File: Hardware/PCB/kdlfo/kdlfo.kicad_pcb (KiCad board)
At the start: 2 copper layers, 93 x 61 mm, 55 parts, among them J1 Synth_power_2x5, J10 AudioJack2, J11 AudioJack2, J12 2 PIN MOLEX HEADER, J13 2 PIN MOLEX CONNECTOR, J2 2 PIN MOLEX HEADER, J3 2 PIN MOLEX HEADER, J4 AudioJack2, J5 2 PIN MOLEX HEADER, J6 2 PIN MOLEX CONNECTOR, J7 2 PIN MOLEX CONNECTOR, J8 2 PIN MOLEX CONNECTOR, J9 3 POSITION PIN HEADER, Q1 J201, Q2 J201, U1 TL074, U2 TL074

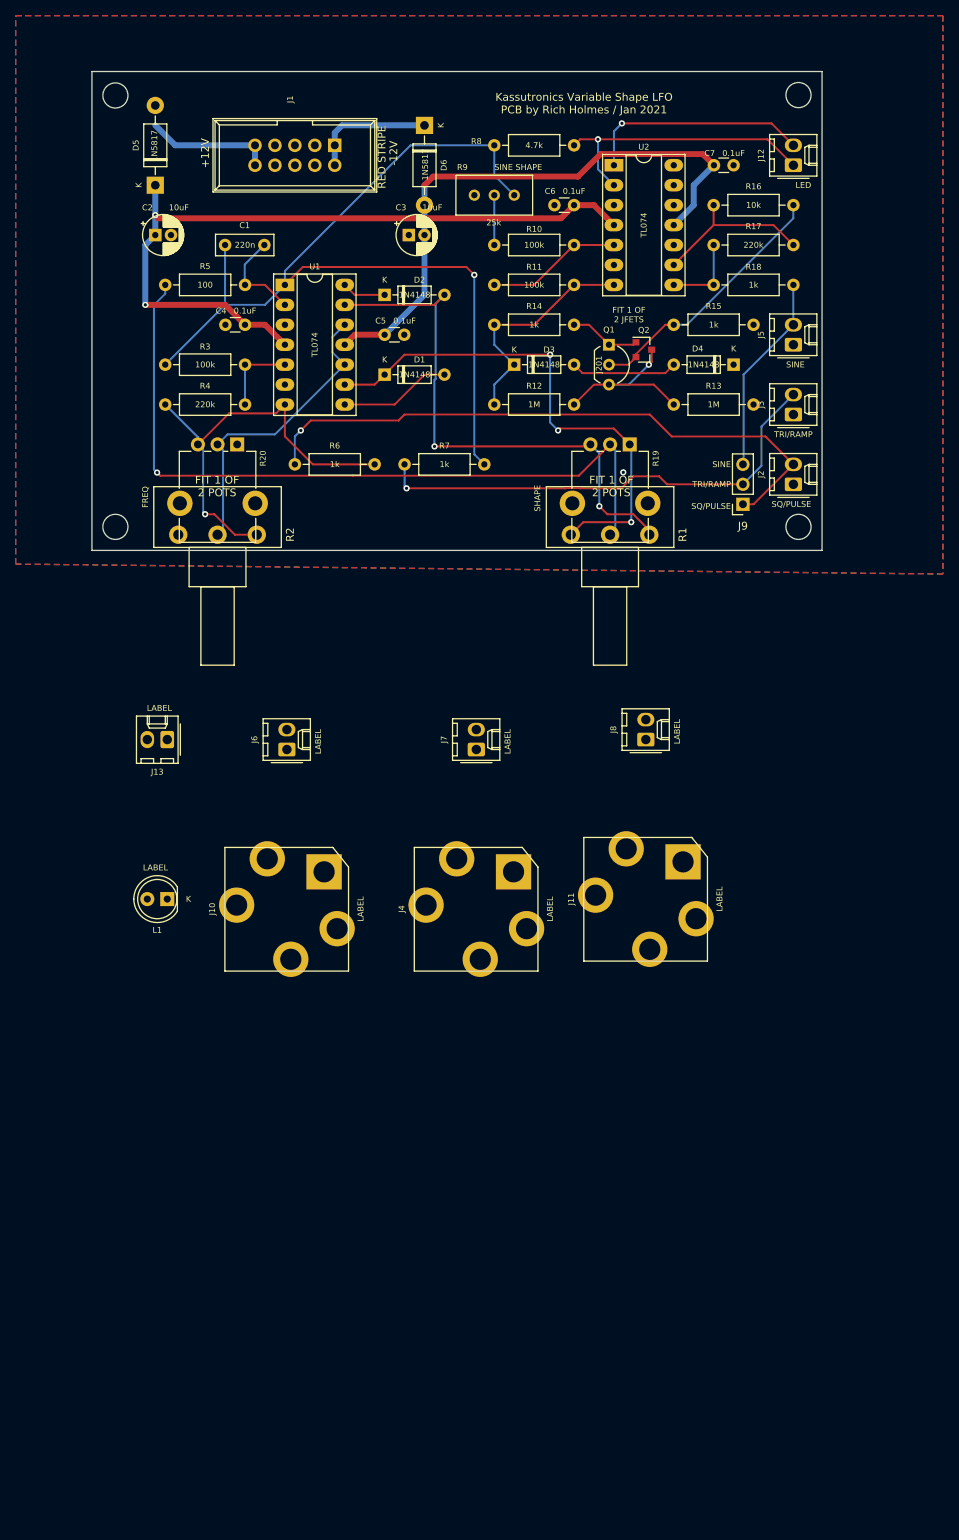
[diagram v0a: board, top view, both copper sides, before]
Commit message: Better .gitignore; rm extraneous footprint library; misc revisions
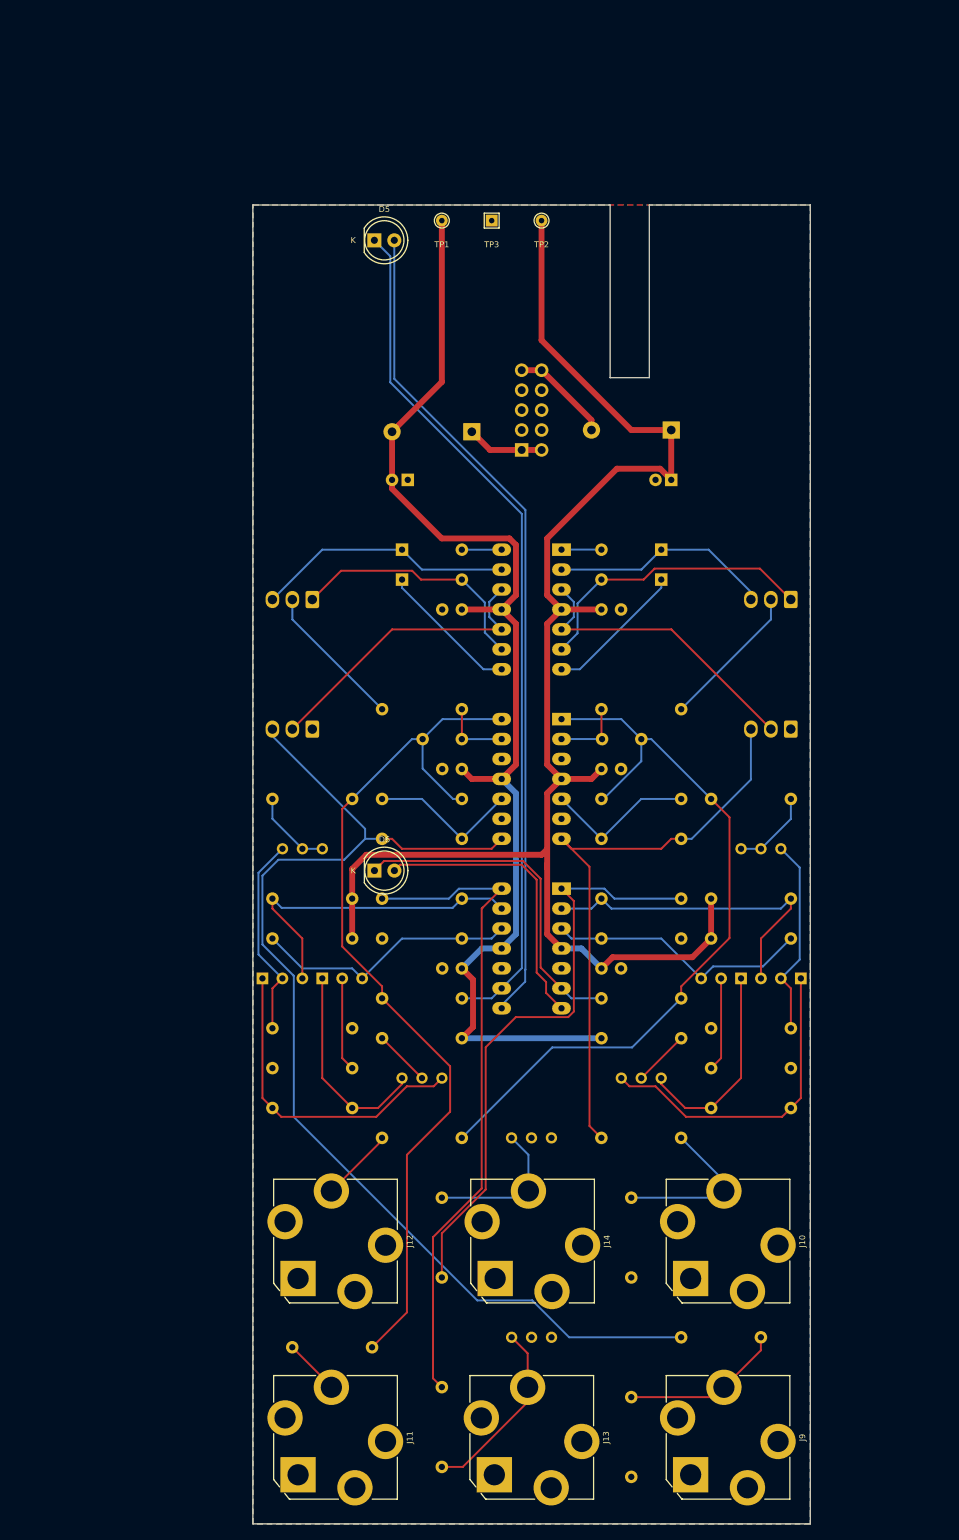
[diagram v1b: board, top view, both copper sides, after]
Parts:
- removed J2: 2 PIN MOLEX HEADER, ao_tht:Molex_KK-254_AE-6410-02A_1x02_P2.54mm_Vertical
- removed J4: AudioJack2, ao_tht:Jack_6.35mm_PJ_629HAN
- removed J6, J8: 2 PIN MOLEX CONNECTOR, ao_tht:Molex_KK-254_AE-6410-02A_1x02_P2.54mm_Vertical
- removed L1: LED_Dual_2pin, ao_tht:LED_D5.0mm
- removed REF** (x4): MountingHole_3.2mm_M3, ao_tht:MountingHole_3.2mm_M3
- added C10: 100nF, ao_tht:C_Disc_D3.0mm_W1.6mm_P2.50mm, B.Cu at (88.6, 130.2)
- added C8: 0.1uF, ao_tht:C_Disc_D3.0mm_W1.6mm_P2.50mm, B.Cu at (88.6, 84.5)
- added C9: 0.1uF, ao_tht:C_Disc_D3.0mm_W1.6mm_P2.50mm, B.Cu at (88.6, 104.8)
- added D7: 1N5817, ao_tht:D_DO-41_SOD81_P10.16mm_Horizontal, B.Cu at (117.8, 61.7)
- added D8: 1N5817, ao_tht:D_DO-41_SOD81_P10.16mm_Horizontal, B.Cu at (92.4, 61.9)
- added GRAF1: Holes, kdlfo:kdlfo_panel_holes, F.Cu at (100.0, 115.0)
- added J14: AudioJack2, ao_tht:Jack_6.35mm_PJ_629HAN, F.Cu at (100.1, 165.0)
- added J15: Synth_power_2x5, ao_tht:Power_Header, B.Cu at (98.7, 64.2)
- added Q3: 2N3904, ao_tht:TO-92_Inline_Wide, B.Cu at (134.3, 131.5)
- added Q4: 2N3904, ao_tht:TO-92_Inline_Wide, B.Cu at (126.7, 131.5)
- added R21: 47k, ao_tht:R_Axial_DIN0207_L6.3mm_D2.5mm_P10.16mm_Horizontal, B.Cu at (67.0, 108.7)
- added R22: 47k, ao_tht:R_Axial_DIN0207_L6.3mm_D2.5mm_P10.16mm_Horizontal, B.Cu at (133.0, 108.7)
- added R23: 20k, ao_tht:R_Axial_DIN0207_L6.3mm_D2.5mm_P10.16mm_Horizontal, B.Cu at (91.1, 126.4)
- added R24: 2k, ao_tht:R_Axial_DIN0207_L6.3mm_D2.5mm_P10.16mm_Horizontal, B.Cu at (88.6, 193.7)
- added R25: 20k, ao_tht:R_Axial_DIN0207_L6.3mm_D2.5mm_P10.16mm_Horizontal, B.Cu at (108.9, 126.4)
- added R26: 2k, ao_tht:R_Axial_DIN0207_L6.3mm_D2.5mm_P10.16mm_Horizontal, B.Cu at (88.6, 159.4)
- added R27: 2.2k, ao_tht:R_Axial_DIN0207_L6.3mm_D2.5mm_P10.16mm_Horizontal, B.Cu at (67.0, 137.9)
- added R28: 2.2k, ao_tht:R_Axial_DIN0207_L6.3mm_D2.5mm_P10.16mm_Horizontal, B.Cu at (77.2, 142.9)
- added R29: 2.2k, ao_tht:R_Axial_DIN0207_L6.3mm_D2.5mm_P10.16mm_Horizontal, B.Cu at (133.0, 137.9)
- added R30: 2.2k, ao_tht:R_Axial_DIN0207_L6.3mm_D2.5mm_P10.16mm_Horizontal, B.Cu at (122.9, 142.9)
- added R31: 390R, ao_tht:R_Axial_DIN0207_L6.3mm_D2.5mm_P10.16mm_Horizontal, B.Cu at (77.2, 148.0)
- added R32: 390R, ao_tht:R_Axial_DIN0207_L6.3mm_D2.5mm_P10.16mm_Horizontal, B.Cu at (122.9, 148.0)
- added R33: 18k, ao_tht:R_Axial_DIN0207_L6.3mm_D2.5mm_P10.16mm_Horizontal, B.Cu at (91.1, 139.1)
- added R34: 18k, ao_tht:R_Axial_DIN0207_L6.3mm_D2.5mm_P10.16mm_Horizontal, B.Cu at (108.9, 139.1)
- added RV10: B50k, ao_tht:Potentiometer_Bourns_3296W_Vertical_standard, B.Cu at (111.4, 144.2)
- added RV5: B50K, ao_tht:Potentiometer_Bourns_3296W_Vertical_standard, B.Cu at (73.3, 115.0)
- added RV6: B50K, ao_tht:Potentiometer_Bourns_3296W_Vertical_standard, B.Cu at (126.7, 115.0)
- added RV7: B5K, ao_tht:Potentiometer_Bourns_3296W_Vertical_standard, B.Cu at (97.5, 177.2)
- added RV8: B5K, ao_tht:Potentiometer_Bourns_3296W_Vertical_standard, B.Cu at (97.5, 151.8)
- added RV9: B50k, ao_tht:Potentiometer_Bourns_3296W_Vertical_standard, B.Cu at (88.6, 144.2)
- added TP1: -12V, ao_tht:TestPoint_THTPad_D1.5mm_Drill0.7mm, F.Cu at (88.6, 35.0)
- added TP2: +12V, ao_tht:TestPoint_THTPad_D1.5mm_Drill0.7mm, F.Cu at (101.3, 35.0)
- added TP3: GND, ao_tht:TestPoint_THTPad_1.5x1.5mm_Drill0.7mm, F.Cu at (94.9, 35.0)
- added U3: TL074, ao_tht:DIP-14_W7.62mm_Socket_LongPads, B.Cu at (103.8, 120.1)
- C1, C3, C4, C5, D1, D2, D3, D4, R16, R4, U1, U2: moved to B.Cu
- C2: value 10uF -> 220n; footprint ao_tht:CP_Radial_D5.0mm_P2.00mm -> ao_tht:C_Rect_L7.2mm_W2.5mm_P5.00mm_FKS2_FKP2_MKS2_MKP2; moved to B.Cu
- C6: value 0.1uF -> 100nF; moved to B.Cu
- C7: value 0.1uF -> 10uF; footprint ao_tht:C_Disc_D3.0mm_W1.6mm_P2.50mm -> ao_tht:CP_Radial_D5.0mm_P2.00mm; moved to B.Cu
- D5, D6: value 1N5817 -> LED_Dual_2pin; footprint ao_tht:D_DO-41_SOD81_P10.16mm_Horizontal -> ao_tht:LED_D5.0mm
- J1: value Synth_power_2x5 -> 3_pin_Molex_header; footprint ao_tht:Power_Header -> ao_tht:Molex_KK-254_AE-6410-03A_1x03_P2.54mm_Vertical; moved to B.Cu
- J12: value 2 PIN MOLEX HEADER -> AudioJack2; footprint ao_tht:Molex_KK-254_AE-6410-02A_1x02_P2.54mm_Vertical -> ao_tht:Jack_6.35mm_PJ_629HAN
- J13: value 2 PIN MOLEX CONNECTOR -> AudioJack2; footprint ao_tht:Molex_KK-254_AE-6410-02A_1x02_P2.54mm_Vertical -> ao_tht:Jack_6.35mm_PJ_629HAN
- J3, J5: value 2 PIN MOLEX HEADER -> 3_pin_Molex_header; footprint ao_tht:Molex_KK-254_AE-6410-02A_1x02_P2.54mm_Vertical -> ao_tht:Molex_KK-254_AE-6410-03A_1x03_P2.54mm_Vertical; moved to B.Cu
- J7: value 2 PIN MOLEX CONNECTOR -> 3_pin_Molex_header; footprint ao_tht:Molex_KK-254_AE-6410-02A_1x02_P2.54mm_Vertical -> ao_tht:Molex_KK-254_AE-6410-03A_1x03_P2.54mm_Vertical; moved to B.Cu
- J9: value 3 POSITION PIN HEADER -> AudioJack2; footprint Connector_PinSocket_2.54mm:PinSocket_1x03_P2.54mm_Vertical -> ao_tht:Jack_6.35mm_PJ_629HAN
- Q1: value J201 -> 2N3904; moved to B.Cu
- Q2: value J201 -> 2N3904; footprint Package_TO_SOT_SMD:SOT-23 -> ao_tht:TO-92_Inline_Wide; moved to B.Cu
- R1: value B100k -> 100; footprint Potentiometer_THT:Potentiometer_Piher_T-16H_Single_Horizontal -> ao_tht:R_Axial_DIN0207_L6.3mm_D2.5mm_P10.16mm_Horizontal; moved to B.Cu
- R10: value 100k -> 2.2k; moved to B.Cu
- R11: value 100k -> 1k; moved to B.Cu
- R12: value 1M -> 1k; moved to B.Cu
- R13: value 1M -> 4.7k; moved to B.Cu
- R14: value 1k -> 4.7k; moved to B.Cu
- R15, R18: value 1k -> 10k; moved to B.Cu
- R17: value 220k -> 20k; moved to B.Cu
- R19: value B100k -> 10k; footprint ao_tht:Potentiometer_Alpha_RD901F-40-00D_Single_Vertical_CircularHoles -> ao_tht:R_Axial_DIN0207_L6.3mm_D2.5mm_P10.16mm_Horizontal; moved to B.Cu
- R2: value A100k -> 100; footprint Potentiometer_THT:Potentiometer_Piher_T-16H_Single_Horizontal -> ao_tht:R_Axial_DIN0207_L6.3mm_D2.5mm_P10.16mm_Horizontal; moved to B.Cu
- R20: value B100k -> 20k; footprint ao_tht:Potentiometer_Alpha_RD901F-40-00D_Single_Vertical_CircularHoles -> ao_tht:R_Axial_DIN0207_L6.3mm_D2.5mm_P10.16mm_Horizontal; moved to B.Cu
- R3: value 100k -> 220k; moved to B.Cu
- R5: value 100 -> 2.7k; moved to B.Cu
- R6: value 1k -> 2.7k; moved to B.Cu
- R7: value 1k -> 100k; moved to B.Cu
- R8: value 4.7k -> 2.2k; moved to B.Cu
- R9: value 25k -> 100k; footprint ao_tht:Potentiometer_Bourns_3296W_Vertical -> ao_tht:R_Axial_DIN0207_L6.3mm_D2.5mm_P10.16mm_Horizontal; moved to B.Cu
- moved R8 159.6 mm to (112.7, 184.8), turned to -90 degrees
- moved R5 154.0 mm to (129.2, 177.2), turned to 180 degrees
- moved J12 149.0 mm to (75.0, 165.0), turned to -90 degrees
- moved R11 140.0 mm to (69.5, 178.5), turned to 0 degrees
- moved R10 121.6 mm to (112.7, 159.4), turned to -90 degrees
- moved J9 118.9 mm to (125.0, 190.0), turned to -90 degrees
- moved R16 104.1 mm to (77.2, 126.4), turned to 180 degrees
- moved J13 100.3 mm to (100.0, 190.0), turned to -90 degrees
- moved R6 98.9 mm to (119.0, 151.8), turned to 180 degrees
- moved C6 97.3 mm to (108.9, 130.2), turned to 0 degrees
- moved D6 95.1 mm to (80.0, 117.8), turned to 0 degrees
- moved R12 94.5 mm to (81.0, 151.8)
- moved R17 93.4 mm to (81.0, 121.4)
- moved Q1 92.0 mm to (65.7, 131.5), turned to 0 degrees
- moved Q2 89.9 mm to (73.3, 131.5)
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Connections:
- C2 pad 1: +12V -> Net-(C2-Pad1)
- C2 pad 2: GND -> Net-(C2-Pad2)
- C3 pad 1: GND -> +12V
- C3 pad 2: -12V -> GND
- C5 pad 1: GND -> +12V
- C5 pad 2: -12V -> GND
- D1 pad 1: Net-(D1-Pad1) -> SHPOTCW
- D2 pad 1: Net-(D2-Pad1) -> SHPOTCW_A
- D3 pad 2: Net-(D3-Pad2) -> SHPOTCCW
- D4 pad 1: GND -> Net-(D4-Pad1)
- D4 pad 2: Net-(D3-Pad2) -> SHPOTCCW_A
- D5 pad 1: +12V -> Net-(D5-Pad1)
- D5 pad 2: /+12_IN -> Net-(D5-Pad2)
- D6 pad 1: /-12_IN -> Net-(D6-Pad1)
- D6 pad 2: -12V -> Net-(D6-Pad2)
- J1 pad 1: /-12_IN -> SHPOTCCW
- J1 pad 2: /-12_IN -> SHPOTW
- J1 pad 3: GND -> SHPOTCW
- J10 pad S: GND1 -> GND
- J10 pad T: /TRIRAMP_P -> /SQPULSE_A
- J11 pad S: GND1 -> GND
- J11 pad T: /SINE_P -> /TRIRAMP
- J3 pad 1: GND -> SHPOTCCW_A
- J3 pad 2: /TRIRAMP -> SHPOTW_A
- J5 pad 2: /SINE -> FRPOTW
- J7 pad 1: /SQPULSE_P -> GND
- J7 pad 2: GND1 -> FRPOTW_A
- Q2 pad 1: Net-(Q1-Pad1) -> Net-(Q2-Pad1)
- Q2 pad 2: Net-(Q1-Pad2) -> Net-(Q2-Pad2)
- Q2 pad 3: Net-(Q1-Pad3) -> Net-(Q2-Pad3)
- R1 pad 1: Net-(D1-Pad1) -> SHPOTW
- R1 pad 2: Net-(R1-Pad2) -> Net-(C1-Pad2)
- R10 pad 1: Net-(R10-Pad1) -> /SQPULSE_A
- R10 pad 2: Net-(R10-Pad2) -> GND
- R11 pad 1: Net-(D3-Pad1) -> /TRIRAMP
- R11 pad 2: Net-(R10-Pad1) -> Net-(C1-Pad1)
- R12 pad 1: Net-(D3-Pad1) -> /TRIRAMP_A
- R12 pad 2: Net-(Q1-Pad3) -> Net-(C2-Pad1)
- R13 pad 1: Net-(Q1-Pad3) -> Net-(D5-Pad1)
- R13 pad 2: GND -> Net-(C1-Pad1)
- R14 pad 1: Net-(D3-Pad1) -> Net-(D6-Pad1)
- R14 pad 2: Net-(Q1-Pad1) -> Net-(C2-Pad1)
- R15 pad 1: Net-(Q1-Pad2) -> +12V
- R15 pad 2: GND -> Net-(Q1-Pad3)
- R16 pad 1: Net-(R16-Pad1) -> +12V
- R16 pad 2: Net-(Q1-Pad2) -> Net-(Q2-Pad3)
- R17 pad 2: Net-(R16-Pad1) -> Net-(Q1-Pad3)
- R18 pad 1: /SINE -> +12V
- R18 pad 2: Net-(R17-Pad1) -> Net-(Q3-Pad3)
- R19 pad 1: Net-(D1-Pad1) -> +12V
- R19 pad 2: Net-(R1-Pad2) -> Net-(Q4-Pad3)
- R2 pad 1: GND -> SHPOTW_A
- R2 pad 2: Net-(R2-Pad2) -> Net-(C2-Pad2)
- R20 pad 1: GND -> Net-(R20-Pad1)
- R20 pad 2: Net-(R2-Pad2) -> Net-(Q3-Pad3)
- R3 pad 1: Net-(R3-Pad1) -> FRPOTCW
- R3 pad 2: Net-(C1-Pad1) -> Net-(R3-Pad2)
- R4 pad 1: Net-(R2-Pad3) -> FRPOTCW_A
- R4 pad 2: Net-(R3-Pad1) -> Net-(R4-Pad2)
- R5 pad 1: Net-(R1-Pad2) -> /SQPULSE
- R5 pad 2: Net-(C1-Pad2) -> FRPOTCW
- R6 pad 1: /SQPULSE -> /SQPULSE_A
- R6 pad 2: Net-(R2-Pad3) -> FRPOTCW_A
- R7 pad 1: /TRIRAMP -> Net-(R3-Pad2)
- R8 pad 1: /LED -> /SQPULSE
- R8 pad 2: Net-(C1-Pad1) -> GND
- R9 pad 1: Net-(C1-Pad1) -> Net-(R4-Pad2)
- R9 pad 2: Net-(R10-Pad2) -> Net-(C2-Pad1)
- U1 pad 1: Net-(C1-Pad1) -> Net-(D2-Pad2)
- U1 pad 10: Net-(R2-Pad2) -> FRPOTW
- U1 pad 12: Net-(R2-Pad2) -> FRPOTW
- U1 pad 13: Net-(D2-Pad2) -> SHPOTCW
- U1 pad 14: Net-(D2-Pad1) -> Net-(D1-Pad2)
- U1 pad 2: Net-(C1-Pad2) -> SHPOTCW_A
- U1 pad 3: GND -> FRPOTW_A
- U1 pad 5: Net-(R3-Pad1) -> FRPOTW_A
- U1 pad 6: GND -> SHPOTCCW_A
- U1 pad 7: Net-(R2-Pad3) -> Net-(D4-Pad1)
- U1 pad 8: Net-(D1-Pad2) -> Net-(D3-Pad1)
- U1 pad 9: Net-(D1-Pad1) -> SHPOTCCW
- U2 pad 1: Net-(J12-Pad2) -> Net-(C2-Pad1)
- U2 pad 10: GND -> Net-(R3-Pad2)
- U2 pad 12: (no net) -> GND
- U2 pad 13: (no net) -> Net-(C1-Pad2)
- U2 pad 14: (no net) -> Net-(C1-Pad1)
- U2 pad 2: /LED -> Net-(C2-Pad2)
- U2 pad 5: Net-(R10-Pad1) -> Net-(R4-Pad2)
- U2 pad 7: Net-(D3-Pad1) -> FRPOTCW_A
- U2 pad 8: Net-(R17-Pad1) -> FRPOTCW
- U2 pad 9: Net-(R16-Pad1) -> GND
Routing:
- net FRPOTCW: track 0.00 -> 145.7 mm
- net Net-(D5-Pad1): track 0.00 -> 109.7 mm
- net Net-(D5-Pad2): track 0.00 -> 106.0 mm
- net Net-(C2-Pad1): track 0.00 -> 97.4 mm
- net Net-(R1-Pad2): track 96.2 -> 0.00 mm, vias 1 -> 0
- net +12V: track 96.0 -> 191.2 mm, vias 2 -> 0
- net -12V: track 75.6 -> 155.3 mm
- net Net-(R20-Pad1): track 0.00 -> 76.8 mm
- net FRPOTCW_A: track 0.00 -> 74.9 mm
- net Net-(R17-Pad1): track 10.2 -> 83.4 mm
- net Net-(D1-Pad1): track 66.8 -> 0.00 mm, vias 3 -> 0
- net Net-(D2-Pad2): track 69.6 -> 5.09 mm, vias 2 -> 0
- net /SQPULSE: track 79.4 -> 20.6 mm, vias 1 -> 0
- net /TRIRAMP: track 61.3 -> 7.16 mm, vias 1 -> 0
- net Net-(R2-Pad3): track 53.9 -> 0.00 mm, vias 1 -> 0
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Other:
- board size 93 x 61 mm -> 71 x 168 mm
- board text removed: "FIT 1 OF 2 JFETS"
- board text removed: "FIT 1 OF 2 POTS"
- board text removed: "Kassutronics Variable Shape LFO PCB by Rich Holmes / Jan 2021"
- board text removed: "SINE"
- board text removed: "SQ/PULSE"
- board text removed: "TRI/RAMP"

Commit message: Reorg schematic, redo layout
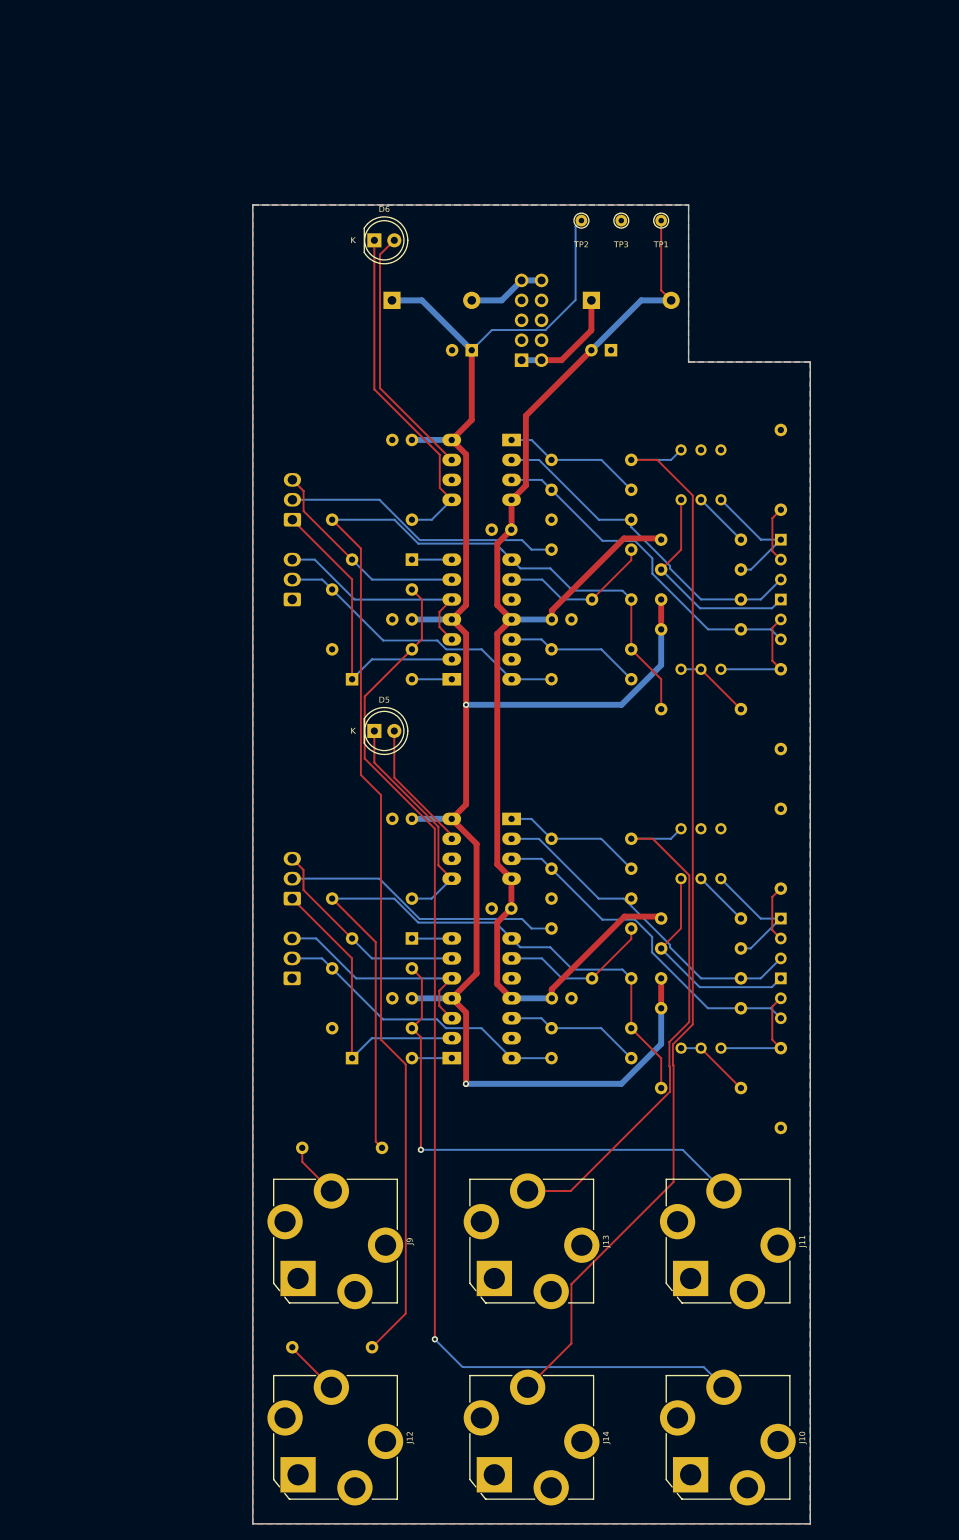
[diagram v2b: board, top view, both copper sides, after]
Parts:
- removed J5: 3_pin_Molex_header, ao_tht:Molex_KK-254_AE-6410-03A_1x03_P2.54mm_Vertical
- added C11: 0.1uF, ao_tht:C_Disc_D3.0mm_W1.6mm_P2.50mm, B.Cu at (84.8, 134.1)
- added C12: 0.1uF, ao_tht:C_Disc_D3.0mm_W1.6mm_P2.50mm, B.Cu at (105.1, 134.1)
- added J2: 3_pin_Molex_header, ao_tht:Molex_KK-254_AE-6410-03A_1x03_P2.54mm_Vertical, B.Cu at (69.5, 131.5)
- added U4: TL072, ao_tht:DIP-8_W7.62mm_Socket_LongPads, B.Cu at (97.5, 111.2)
- C1, C2: footprint ao_tht:C_Rect_L7.2mm_W2.5mm_P5.00mm_FKS2_FKP2_MKS2_MKP2 -> ao_tht:C_Rect_L7.2mm_W7.2mm_P5.00mm_FKS2_FKP2_MKS2_MKP2
- C10, C6: value 100nF -> 0.1uF
- C3, C7: footprint ao_tht:CP_Radial_D5.0mm_P2.00mm -> ao_tht:CP_Radial_D6.3mm_P2.50mm
- D1, D2, D3, D4: footprint ao_tht:D_DO-35_SOD27_P7.62mm_Horizontal -> Diode_THT:D_DO-35_SOD27_P7.62mm_Horizontal
- R1: value 100 -> 47k
- R11: value 1k -> 100k
- R13: value 4.7k -> 10k
- R15: value 10k -> 18k
- R16: value 10k -> 2.2k
- R17: value 20k -> 220k
- R21: value 47k -> 20k
- R23: value 20k -> 2.7k
- R24: value 2k -> 20k
- R28: value 2.2k -> 4.7k
- R3: value 220k -> 100
- R31: value 390R -> 1k
- R33: value 18k -> 2k
- R5: value 2.7k -> 2.2k
- R7: value 100k -> 10k
- R8: value 2.2k -> 390R
- RV7: value B5K -> B50k
- RV9: value B50k -> B5K
- TP3: footprint ao_tht:TestPoint_THTPad_1.5x1.5mm_Drill0.7mm -> ao_tht:TestPoint_THTPad_D1.5mm_Drill0.7mm
- U2: value TL074 -> TL072; footprint ao_tht:DIP-14_W7.62mm_Socket_LongPads -> ao_tht:DIP-8_W7.62mm_Socket_LongPads
- moved R26 97.0 mm to (112.7, 65.5), turned to 180 degrees
- moved RV8 90.3 mm to (119.0, 64.2)
- moved D6 80.3 mm to (80.0, 37.5)
- moved R24 79.9 mm to (112.7, 117.5), turned to 180 degrees
- moved R6 77.8 mm to (84.8, 82.0)
- moved R10 75.2 mm to (84.8, 89.6), turned to 180 degrees
- moved RV10 74.1 mm to (119.0, 70.5)
- moved R30 71.7 mm to (131.8, 71.8), turned to 90 degrees
- moved R32 68.7 mm to (126.7, 79.4), turned to 180 degrees
- moved R1 66.5 mm to (126.7, 145.5), turned to 180 degrees
- moved Q1 66.0 mm to (131.8, 131.5), turned to -90 degrees
- moved J7 65.6 mm to (69.5, 83.2), turned to 90 degrees
- moved R14 65.6 mm to (84.8, 73.1), turned to 180 degrees
- moved D1 65.1 mm to (77.1, 141.7)
- moved J3 64.3 mm to (69.5, 73.1), turned to 90 degrees
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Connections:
- net /SINE_A renamed /LFO A/SINE
- net /SINE_ROUND_A renamed /LFO A/SINE_ROUND
- net /SINE_SYM_A renamed /LFO A/SINE_SYM
- net /SQPULSE_A renamed /LFO A/SQPULSE
- net /TRIRAMP_A renamed /LFO A/TRIRAMP
- net SHPOTW_A renamed /LFO A/SHPOTW
- C6 pad 1: +12V -> GND
- C6 pad 2: GND -> -12V
- C9 pad 1: GND -> +12V
- C9 pad 2: -12V -> GND
- D1 pad 1: SHPOTCW -> /LFO B/SHPOTCW
- D2 pad 1: SHPOTCW_A -> /LFO A/SHPOTCW
- D3 pad 2: SHPOTCCW -> /LFO B/SHPOTCCW
- D4 pad 2: SHPOTCCW_A -> /LFO A/SHPOTCCW
- J1 pad 1: SHPOTCCW -> /LFO B/SHPOTCW
- J1 pad 2: SHPOTW -> /LFO B/SHPOTW
- J1 pad 3: SHPOTCW -> /LFO B/SHPOTCCW
- J11 pad T: /TRIRAMP -> /LFO B/SQPULSE
- J13 pad T: /SINE -> /LFO B/SINE
- J3 pad 1: SHPOTCCW_A -> /LFO A/SHPOTCW
- J3 pad 3: SHPOTCW_A -> /LFO A/SHPOTCCW
- J7 pad 2: FRPOTW_A -> /LFO A/FRPOTCW
- J7 pad 3: FRPOTCW_A -> /LFO A/FRPOTW
- J9 pad T: /SQPULSE -> /LFO B/TRIRAMP
- R1 pad 1: SHPOTW -> /LFO B/SINE_ROUND
- R1 pad 2: Net-(C1-Pad2) -> Net-(C1-Pad1)
- R11 pad 1: /TRIRAMP -> Net-(R11-Pad1)
- R13 pad 1: Net-(D5-Pad1) -> +12V
- R13 pad 2: Net-(C1-Pad1) -> Net-(Q2-Pad3)
- R15 pad 1: +12V -> -12V
- R15 pad 2: Net-(Q1-Pad3) -> /LFO B/SINE_SYM
- R16 pad 1: +12V -> Net-(Q2-Pad2)
- R16 pad 2: Net-(Q2-Pad3) -> GND
- R17 pad 1: Net-(R17-Pad1) -> /LFO B/FRPOTCW
- R17 pad 2: Net-(Q1-Pad3) -> Net-(R11-Pad1)
- R21 pad 1: /SINE_ROUND -> Net-(Q2-Pad3)
- R21 pad 2: Net-(C1-Pad1) -> GND
- R23 pad 1: Net-(Q2-Pad3) -> /LFO B/SQPULSE
- R23 pad 2: GND -> /LFO B/FRPOTCW
- R24 pad 1: /SINE -> Net-(R24-Pad1)
- R24 pad 2: Net-(R17-Pad1) -> Net-(Q1-Pad3)
- R27 pad 1: Net-(Q1-Pad2) -> /LFO B/SQPULSE
- R28 pad 1: Net-(Q2-Pad2) -> Net-(D5-Pad1)
- R28 pad 2: GND -> Net-(C1-Pad1)
- R3 pad 1: FRPOTCW -> /LFO B/SHPOTW
- R3 pad 2: Net-(R3-Pad2) -> Net-(C1-Pad2)
- R31 pad 1: Net-(Q2-Pad1) -> /LFO B/TRIRAMP
- R31 pad 2: Net-(Q1-Pad1) -> Net-(C1-Pad1)
- R33 pad 1: -12V -> /LFO B/SINE
- R33 pad 2: /SINE_SYM -> Net-(R24-Pad1)
- R4 pad 1: FRPOTCW_A -> /LFO A/FRPOTCW
- R5 pad 1: /SQPULSE -> Net-(Q1-Pad2)
- R5 pad 2: FRPOTCW -> GND
- R6 pad 2: FRPOTCW_A -> /LFO A/FRPOTCW
- R7 pad 1: Net-(R3-Pad2) -> +12V
- R7 pad 2: Net-(C1-Pad1) -> Net-(Q1-Pad3)
- R8 pad 1: /SQPULSE -> Net-(Q2-Pad1)
- R8 pad 2: GND -> Net-(Q1-Pad1)
- RV5 pad 1: /SINE_ROUND -> /LFO B/SINE_ROUND
- RV5 pad 2: /SINE_ROUND -> /LFO B/SINE_ROUND
- RV7 pad 1: /SINE -> Net-(Q1-Pad1)
- RV7 pad 2: GND -> /LFO B/SINE_SYM
- RV7 pad 3: GND -> Net-(Q2-Pad1)
- RV9 pad 1: Net-(Q1-Pad1) -> /LFO B/SINE
- RV9 pad 2: /SINE_SYM -> GND
- RV9 pad 3: Net-(Q2-Pad1) -> GND
- U1 pad 10: FRPOTW -> GND
- U1 pad 12: FRPOTW -> Net-(R4-Pad2)
- U1 pad 13: SHPOTCW -> GND
- U1 pad 14: Net-(D1-Pad2) -> /LFO A/FRPOTCW
- U1 pad 2: SHPOTCW_A -> /LFO A/SHPOTCW
- U1 pad 3: FRPOTW_A -> /LFO A/FRPOTW
- U1 pad 5: FRPOTW_A -> /LFO A/FRPOTW
- U1 pad 6: SHPOTCCW_A -> /LFO A/SHPOTCCW
- U1 pad 8: Net-(D3-Pad1) -> Net-(C2-Pad1)
- U1 pad 9: SHPOTCCW -> Net-(C2-Pad2)
- U2 pad 1: Net-(C2-Pad1) -> Net-(R20-Pad1)
- U2 pad 2: Net-(C2-Pad2) -> Net-(Q4-Pad3)
- U2 pad 3: GND -> Net-(Q3-Pad3)
- U2 pad 4: +12V -> -12V
- U2 pad 5: Net-(R4-Pad2) -> Net-(D6-Pad1)
- U2 pad 7: FRPOTCW_A -> Net-(D6-Pad2)
- U2 pad 8: FRPOTCW -> +12V
- U3 pad 1: Net-(R20-Pad1) -> Net-(D1-Pad2)
- U3 pad 12: Net-(Q2-Pad3) -> Net-(R11-Pad1)
- U3 pad 13: Net-(Q1-Pad3) -> GND
- U3 pad 14: Net-(R17-Pad1) -> /LFO B/FRPOTCW
- U3 pad 2: Net-(Q3-Pad3) -> /LFO B/SHPOTCW
- U3 pad 3: Net-(Q4-Pad3) -> /LFO B/FRPOTW
- U3 pad 5: GND -> /LFO B/FRPOTW
- U3 pad 6: Net-(D6-Pad1) -> /LFO B/SHPOTCCW
- U3 pad 7: Net-(D6-Pad2) -> Net-(D3-Pad1)
- U3 pad 8: Net-(D5-Pad2) -> Net-(C1-Pad1)
- U3 pad 9: Net-(D5-Pad1) -> Net-(C1-Pad2)
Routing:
- net FRPOTCW: track 145.7 -> 0.00 mm
- net /LFO A/SQPULSE: track 21.2 -> 142.1 mm, vias 0 -> 1
- net /LFO A/SINE: track 19.0 -> 139.0 mm
- net Net-(D5-Pad2): track 106.0 -> 16.3 mm
- net Net-(R17-Pad1): track 83.4 -> 0.00 mm
- net Net-(D5-Pad1): track 109.7 -> 29.0 mm
- net FRPOTCW_A: track 74.9 -> 0.00 mm
- net Net-(C2-Pad1): track 97.4 -> 168.9 mm
- net /LFO B/SINE: track 0.00 -> 68.2 mm
- net /LFO B/SQPULSE: track 0.00 -> 65.4 mm, vias 0 -> 1
- net Net-(R20-Pad1): track 76.8 -> 17.9 mm
- net +12V: track 191.2 -> 230.9 mm, vias 0 -> 2
- net FRPOTW_A: track 38.3 -> 0.00 mm
- net FRPOTW: track 38.3 -> 0.00 mm
- net /LFO B/FRPOTCW: track 0.00 -> 38.3 mm
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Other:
- outline, holes or cut-outs redrawn
